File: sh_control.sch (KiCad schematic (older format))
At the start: 62 parts, among them IC5 LM317MDCY, J1 12401598E4#2A, J2 10129381-906001BLF, J3 10129381-906001BLF

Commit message: deleted all, beginning of eval board
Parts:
- removed C13: 1 uF, SamacSys_Parts:CAPC3216X210N, symbol SamacSys_Parts:SH31B105K500CT
- removed C14, C18, C19, C20, C21, C22, C23: 10 uF, SamacSys_Parts:CAPC3216X180N, symbol SamacSys_Parts:CL31A106KPHNNNE
- removed C15, C17: 0.1 uF, SamacSys_Parts:CAPC3216X88N, symbol SamacSys_Parts:C1206C104K5RAC7411
- removed C16, C24, C25, C26, C27: 100 uF, SamacSys_Parts:CAPPRD250W45D630H500, symbol SamacSys_Parts:10ML100MEFC6.3X5
- removed D1, D2, D3: FM4002-W, SamacSys_Parts:DIOM5025X231N, symbol SamacSys_Parts:FM4002-W
- removed DN_1, DN_2, DN_3, DN_4, DP_1, DP_2, DP_3, DP_4, GND1, GND2, GND_1, GND_2, GND_3, GND_4, LED_VCC_in1, LED_VCC_out1, VCC_1, VCC_2, VCC_3, VCC_4: TestPoint, TestPoint:TestPoint_Pad_2.0x2.0mm, symbol Connector:TestPoint
- removed F1, F2: Fuse, SamacSys_Parts:FUSC4632X85N, symbol SamacSys_Parts:MF-MSMF050-2
- removed H1, H2, H3, H4: MountingHole, MountingHole:MountingHole_3.2mm_M3, symbol Mechanical:MountingHole
- removed IC5: LM317MDCY, SamacSys_Parts:SOT230P700X180-4N, symbol SamacSys_Parts:LM317MDCY
- removed J1: 12401598E4#2A, usb c connector:AMPHENOL_12401598E4#2A, symbol 12401598E4_2A:12401598E4#2A
- removed J2, J3: 10129381-906001BLF, SamacSys_Parts:HDRV6W67P254_2X3_762X483X858P, symbol SamacSys_Parts:10129381-906001BLF
- removed LED4, LED5, LED6, LED7, LED8, LED9: COM-13667, SamacSys_Parts:COM13667, symbol SamacSys_Parts:COM-13667
- removed R31, R33: 390 R, SamacSys_Parts:RESC3216X60N, symbol SamacSys_Parts:CRCW1206390RFKEA
- removed R32: 240 R, SamacSys_Parts:RESC3216X75N, symbol SamacSys_Parts:CR1206-FX-2400ELF
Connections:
- net labels removed: +3.3V, +5V, DN_1, DN_2, DN_3, DN_4, DN_hub, DP_1, DP_2, DP_3, DP_4, DP_hub, USB_GND, USB_vbus
- wire segments 213 -> 10
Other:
- moved on the sheet: PB0, PC5, PD2, PD3, PD7

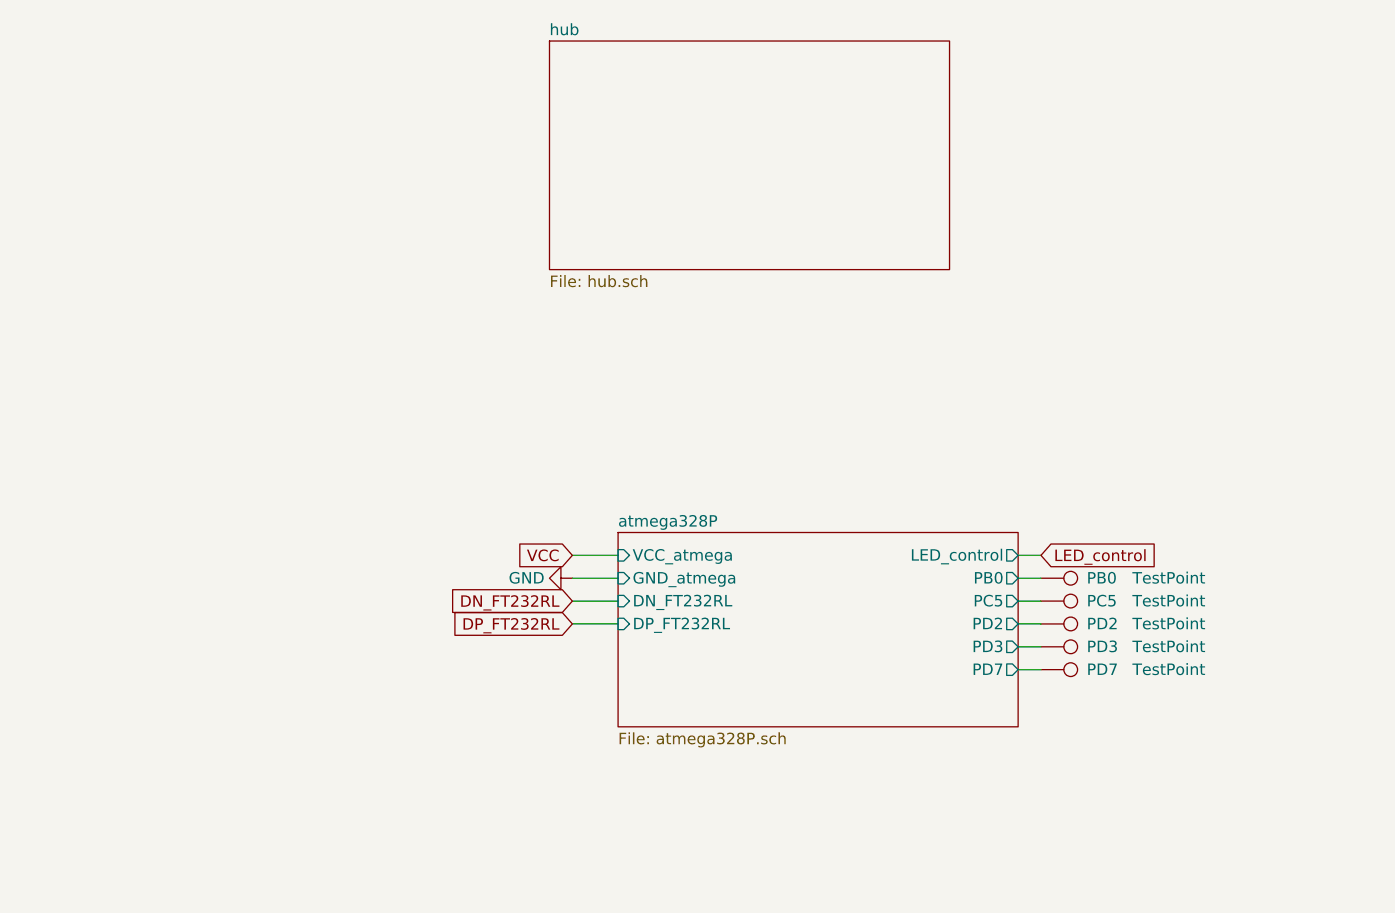
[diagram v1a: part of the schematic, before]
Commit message: hub schematic finished
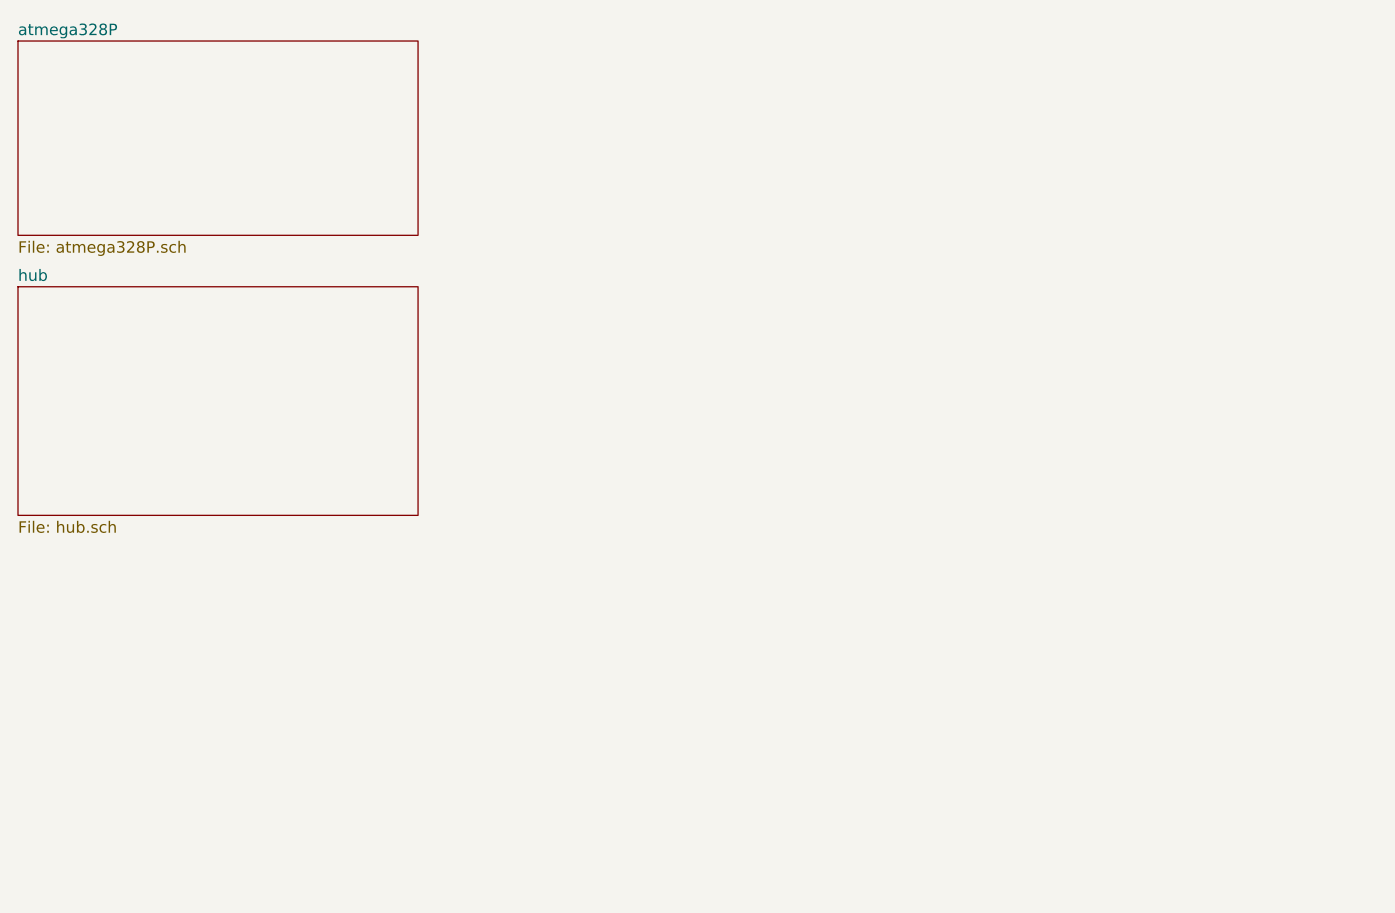
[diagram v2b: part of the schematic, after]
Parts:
- removed PB0, PC5, PD2, PD3, PD7: TestPoint, TestPoint:TestPoint_Pad_2.0x2.0mm, symbol Connector:TestPoint
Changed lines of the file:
@@
 $EndDescr
 $Sheet
-S 3250 2850 1750 850
+S 625  700  1750 850
 U 60A55B56
 F0 "atmega328P" 50
 F1 "atmega328P.sch" 50
-F2 "VCC_atmega" I L 3250 2950 50
-F3 "GND_atmega" I L 3250 3050 50
-F4 "LED_control" O R 5000 2950 50
-F5 "PB0" O R 5000 3050 50
-F6 "PC5" O R 5000 3150 50
-F7 "PD7" O R 5000 3450 50
-F8 "PD3" O R 5000 3350 50
-F9 "PD2" O R 5000 3250 50
-F10 "DN_FT232RL" I L 3250 3150 50
-F11 "DP_FT232RL" I L 3250 3250 50
 $EndSheet
-Text GLabel 5100 2950 2    50   Input ~ 0
-LED_control
-Wire Wire Line
-	5000 2950 5100 2950
 $Comp
 L power:GND #PWR0139
@@
 	1    0    0    -1
 $EndComp
-Text GLabel 3050 3150 0    50   Input ~ 0
-DN_FT232RL
-Text GLabel 3050 3250 0    50   Input ~ 0
-DP_FT232RL
-Wire Wire Line
-	3050 3150 3250 3150
-Wire Wire Line
-	3050 3250 3250 3250
-$Comp
-L power:GND #PWR0148
-U 1 1 6076ABFB
-P 3050 3050
-F 0 "#PWR0148" H 3050 2800 50  0001 C CNN
-F 1 "GND" V 3050 2850 50  0000 C CNN
-F 2 "" H 3050 3050 50  0001 C CNN
-F 3 "" H 3050 3050 50  0001 C CNN
-	1    3050 3050
-	0    1    1    0
-$EndComp
-Wire Wire Line
-	3050 3050 3250 3050
-Text GLabel 3050 2950 0    50   Input ~ 0
-VCC
-Wire Wire Line
-	3050 2950 3250 2950
-$Comp
-L Connector:TestPoint PB0
-U 1 1 60793E9F
-P 5100 3050
-F 0 "PB0" V 5100 3250 50  0000 L CNN
-F 1 "TestPoint" V 5100 3450 50  0000 L CNN
-F 2 "TestPoint:TestPoint_Pad_2.0x2.0mm" H 5300 3050 50  0001 C CNN
-F 3 "~" H 5300 3050 50  0001 C CNN
-	1    5100 3050
-	0    1    1    0
-$EndComp
-$Comp
-L Connector:TestPoint PC5
-U 1 1 607EDBC8
-P 5100 3150
-F 0 "PC5" V 5100 3350 50  0000 L CNN
-F 1 "TestPoint" V 5100 3550 50  0000 L CNN
-F 2 "TestPoint:TestPoint_Pad_2.0x2.0mm" H 5300 3150 50  0001 C CNN
-F 3 "~" H 5300 3150 50  0001 C CNN
-	1    5100 3150
-	0    1    1    0
-$EndComp
-$Comp
-L Connector:TestPoint PD2
-U 1 1 607F7B9C
-P 5100 3250
-F 0 "PD2" V 5100 3450 50  0000 L CNN
-F 1 "TestPoint" V 5100 3650 50  0000 L CNN
-F 2 "TestPoint:TestPoint_Pad_2.0x2.0mm" H 5300 3250 50  0001 C CNN
-F 3 "~" H 5300 3250 50  0001 C CNN
-	1    5100 3250
-	0    1    1    0
-$EndComp
-$Comp
-L Connector:TestPoint PD3
-U 1 1 608018E8
-P 5100 3350
-F 0 "PD3" V 5100 3550 50  0000 L CNN
-F 1 "TestPoint" V 5100 3750 50  0000 L CNN
-F 2 "TestPoint:TestPoint_Pad_2.0x2.0mm" H 5300 3350 50  0001 C CNN
-F 3 "~" H 5300 3350 50  0001 C CNN
-	1    5100 3350
-	0    1    1    0
-$EndComp
-$Comp
-L Connector:TestPoint PD7
-U 1 1 6080B6FE
-P 5100 3450
-F 0 "PD7" V 5100 3650 50  0000 L CNN
-F 1 "TestPoint" V 5100 3850 50  0000 L CNN
-F 2 "TestPoint:TestPoint_Pad_2.0x2.0mm" H 5300 3450 50  0001 C CNN
-F 3 "~" H 5300 3450 50  0001 C CNN
-	1    5100 3450
-	0    1    1    0
-$EndComp
-Wire Wire Line
-	5000 3050 5100 3050
-Wire Wire Line
-	5000 3150 5100 3150
-Wire Wire Line
-	5100 3250 5000 3250
-Wire Wire Line
-	5000 3350 5100 3350
-Wire Wire Line
-	5100 3450 5000 3450
 $Sheet
-S 2950 700  1750 1000
+S 625  1775 1750 1000
 U 606F0FFF
 F0 "hub" 50

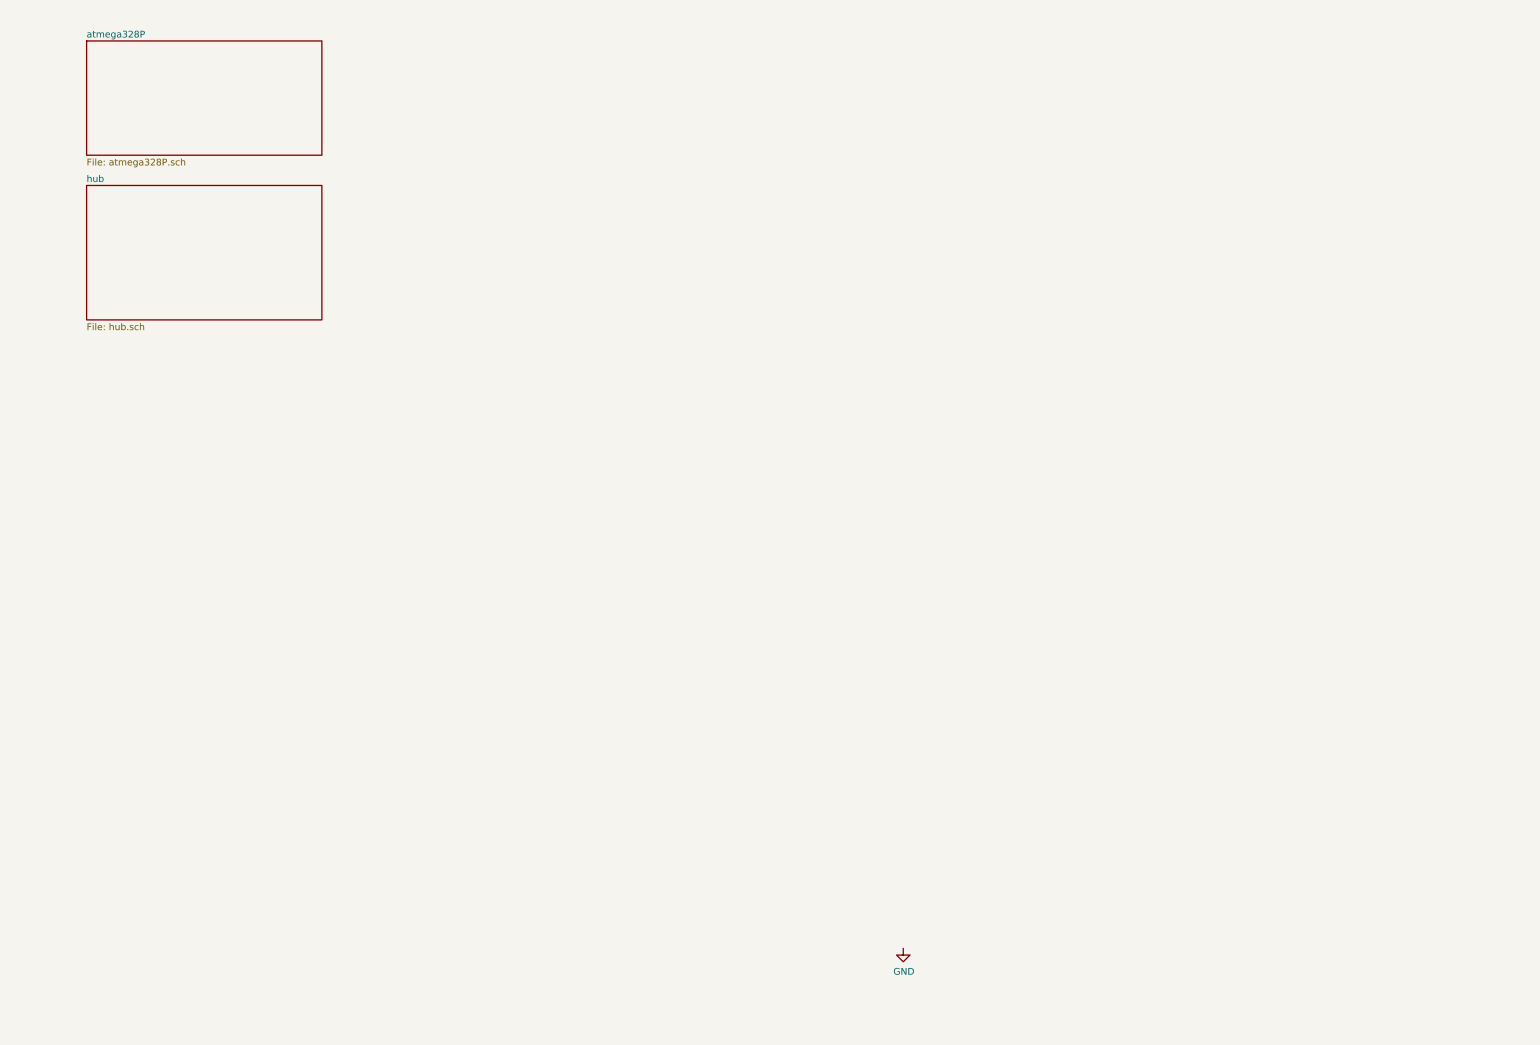
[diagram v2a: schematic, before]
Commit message: split in two boards from now on
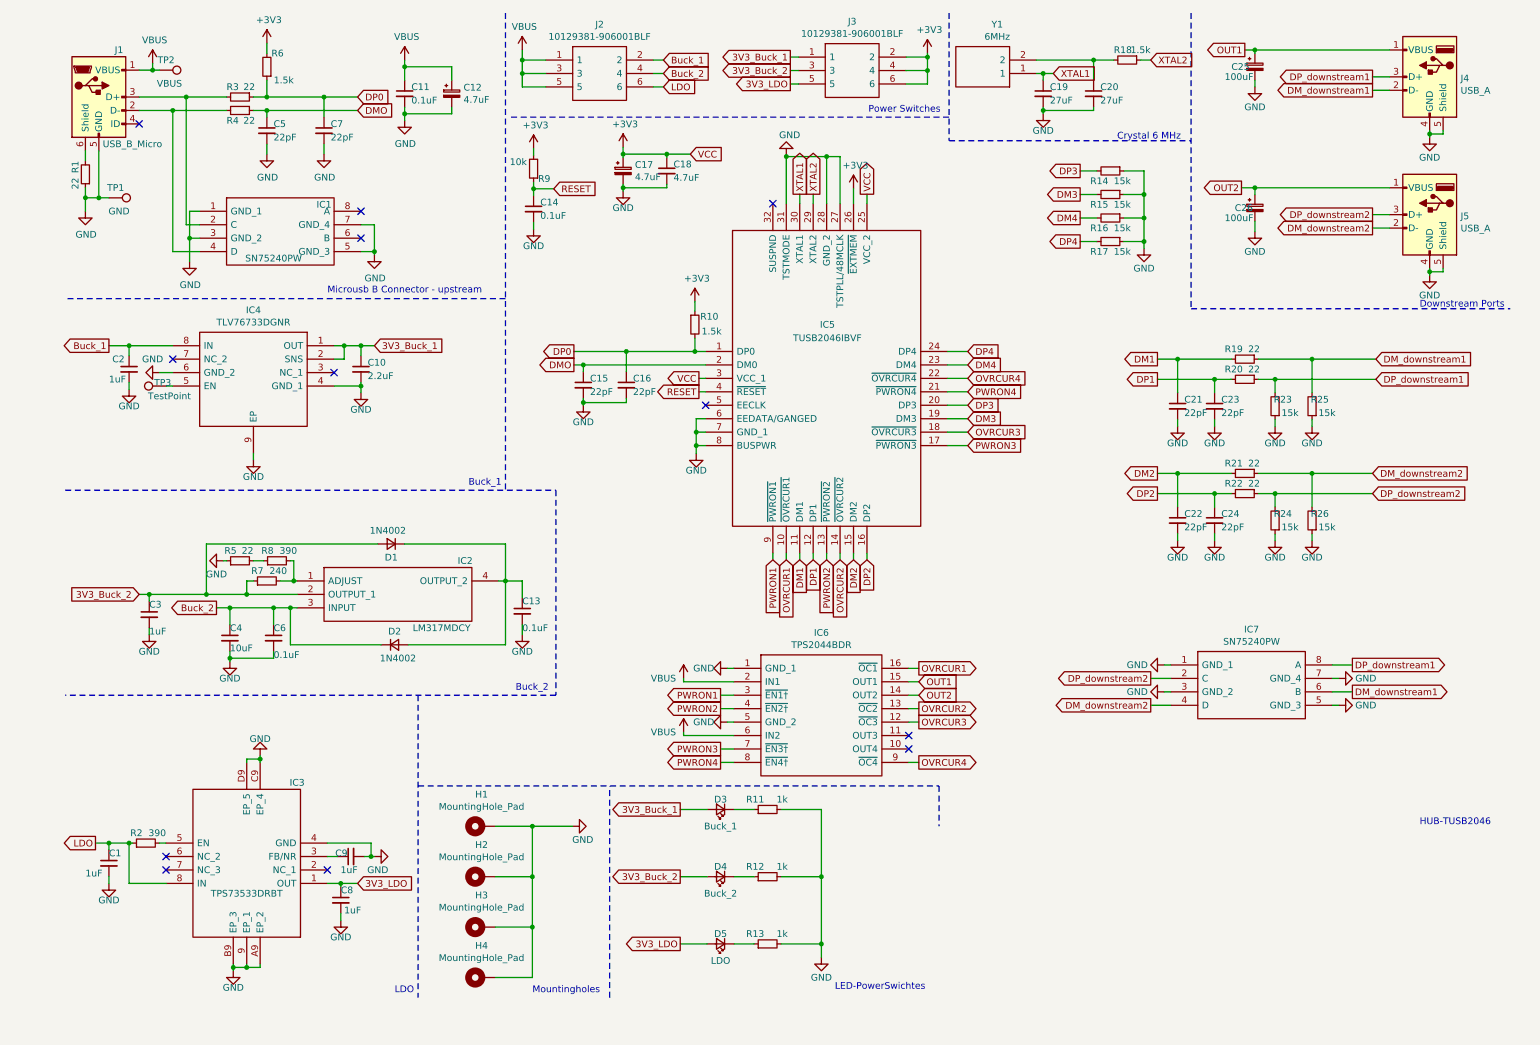
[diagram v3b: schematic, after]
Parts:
- added C1, C2, C3, C8, C9: 1uF, storage:C_1uF, symbol Device:C_Small
- added C10: 2.2uF, storage:C_2.2F, symbol Device:C_Small
- added C11, C13, C14, C6: 0.1uF, storage:C_0.1uF, symbol Device:C_Small
- added C12, C17: 4.7uF, storage:C_4.7uF, symbol Device:CP_Small
- added C15, C16, C21, C22, C23, C24, C5, C7: 22pF, storage:C_22pF, symbol Device:C_Small
- added C18: 4.7uF, storage:C_4.7uF, symbol Device:C_Small
- added C19, C20: 27uF, storage:C_27pF, symbol Device:C_Small
- added C25, C26: 100uF, storage:C_100uF, symbol Device:CP_Small
- added C4: 10uF, storage:C_10uF, symbol Device:C_Small
- added D1, D2: 1N4002, storage:D_1N4002, symbol Device:D_Small
- added D3: Buck_1, SamacSys_Parts:LEDC3214X78N, symbol Device:LED_Small
- added D4: Buck_2, SamacSys_Parts:LEDC3214X78N, symbol Device:LED_Small
- added D5: LDO, SamacSys_Parts:LEDC3214X78N, symbol Device:LED_Small
- added H1, H2, H3, H4: MountingHole_Pad, MountingHole:MountingHole_3.2mm_M3_Pad_Via, symbol Mechanical:MountingHole_Pad
- added IC1, IC7: SN75240PW, SamacSys_Parts:SOP65P640X120-8N, symbol SamacSys_Parts:SN75240PW
- added IC2: LM317MDCY, SamacSys_Parts:SOT230P700X180-4N, symbol SamacSys_Parts:LM317MDCY
- added IC3: TPS73533DRBT, SamacSys_Parts:TPS73533DRBT, symbol SamacSys_Parts:TPS73533DRBT
- added IC4: TLV76733DGNR, SamacSys_Parts:SOP65P490X110-9N, symbol SamacSys_Parts:TLV76733DGNR
- added IC5: TUSB2046IBVF, SamacSys_Parts:QFP80P900X900X160-32N, symbol SamacSys_Parts:TUSB2046IBVF
- added IC6: TPS2044BDR, SamacSys_Parts:SOIC127P600X175-16N, symbol SamacSys_Parts:TPS2044BDR
- added J1: USB_B_Micro, Connector_USB:USB_Micro-B_Molex-105017-0001, symbol Connector:USB_B_Micro
- added J2, J3: 10129381-906001BLF, SamacSys_Parts:HDRV6W67P254_2X3_762X483X858P, symbol SamacSys_Parts:10129381-906001BLF
- added J4, J5: USB_A, Connector_USB:USB_A_Molex_67643_Horizontal, symbol Connector:USB_A
- added R1, R19, R20, R21, R22, R3, R4, R5: 22, storage:R_22, symbol Device:R_Small
- added R10, R18, R6: 1.5k, storage:R_1K5, symbol Device:R_Small
- added R11, R12, R13: 1k, storage:R_1K, symbol Device:R_Small
- added R14, R15, R16, R17, R23, R24, R25, R26: 15k, storage:R_15K, symbol Device:R_Small
- added R2, R8: 390, storage:R_390, symbol Device:R_Small
- added R7: 240, storage:R_240, symbol Device:R_Small
- added R9: 10k, storage:R_10K, symbol Device:R_Small
- added TP1: GND, TestPoint:TestPoint_Pad_D2.5mm, symbol Connector:TestPoint
- added TP2: VBUS, TestPoint:TestPoint_Pad_D2.5mm, symbol Connector:TestPoint
- added TP3: TestPoint, TestPoint:TestPoint_Pad_D2.5mm, symbol Connector:TestPoint
- added Y1: 6MHz, SamacSys_Parts:LFXTAL036567BULK, symbol SamacSys_Parts:LFXTAL036567BULK
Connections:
- net GND: now also C1.2, C10.2, C11.2, C12.2, C13.2, C14.2, C15.2, C16.2, C17.2, C18.2, C19.2, C2.2, C20.2, C21.2, C22.2, C23.2, C24.2, C25.2, C26.2, C3.2, C4.2, C5.2, C6.2, C7.2, C8.2, C9.2, H1.1, H2.1, H3.1, H4.1, IC1.1 (GND_1), IC1.3 (GND_2), IC1.5 (GND_3), IC1.7 (GND_4), IC3.4 (GND), IC3.9 (EP_1), IC3.A9 (EP_2), IC3.B9 (EP_3), IC3.C9 (EP_4), IC3.D9 (EP_5), IC4.4 (GND_1), IC4.6 (GND_2), IC4.9 (EP), IC5.27 (TSTPLL/48MCLK), IC5.28 (GND_2), IC5.31 (TSTMODE), IC5.6 (EEDATA/GANGED), IC5.7 (GND_1), IC5.8 (BUSPWR), IC6.1 (GND_1), IC6.5 (GND_2), IC7.1 (GND_1), IC7.3 (GND_2), IC7.5 (GND_3), IC7.7 (GND_4), J1.5 (GND), J4.4 (GND), J4.5 (Shield), J5.4 (GND), J5.5 (Shield), R1.1, R11.2, R12.2, R13.2, R14.1, R15.1, R16.1, R17.1, R23.1, R24.1, R25.1, R26.1, R5.1, TP1.1
- new net: IC4.5 (EN), TP3.1
- new net: IC2.1 (ADJUST), R7.2, R8.2
- new net: C13.1, D1.1 (K), D2.2 (A), IC2.4 (OUTPUT_2)
- new net: R5.2, R8.1
- new net: C9.1, IC3.3 (FB/NR)
- new net: IC3.5 (EN), R2.2
- new net: C20.1, R18.2, Y1.2
- new net: J1.6 (Shield), R1.2
- new net: IC1.2 (C), J1.3 (D+), R3.2
- new net: IC1.4 (D), J1.2 (D-), R4.2
- new net: D3.1 (K), R11.1
- new net: D4.1 (K), R12.1
- new net: D5.1 (K), R13.1
- new net +3V3: C17.1, C18.1, IC5.25 (VCC_2), IC5.26 (~EXTMEM), IC5.3 (VCC_1), J3.2, J3.4, J3.6, R10.1, R6.2, R9.2
- new net 3V3_Buck_1: C10.1, D3.2 (A), IC4.1 (OUT), IC4.2 (SNS), J3.1
- new net 3V3_Buck_2: C3.1, D1.2 (A), D4.2 (A), IC2.2 (OUTPUT_1), J3.3, R7.1
- new net 3V3_LDO: C8.1, D5.2 (A), IC3.1 (OUT), J3.5
- new net Buck_1: C2.1, IC4.8 (IN), J2.2
- new net Buck_2: C4.1, C6.1, D2.1 (K), IC2.3 (INPUT), J2.4
- new net DM1: C21.1, IC5.11 (DM1), R19.2
- new net DM2: C22.1, IC5.15 (DM2), R21.2
- new net DM3: IC5.19 (DM3), R15.2
- new net DM4: IC5.23 (DM4), R16.2
- new net DMO: C15.1, C5.1, IC5.2 (DM0), R4.1
- new net DM_downstream1: IC7.6 (B), J4.2 (D-), R19.1, R25.2
- new net DM_downstream2: IC7.4 (D), J5.2 (D-), R21.1, R26.2
- new net DP0: C16.1, C7.1, IC5.1 (DP0), R10.2, R3.1, R6.1
- new net DP1: C23.1, IC5.12 (DP1), R20.2
- new net DP2: C24.1, IC5.16 (DP2), R22.2
- new net DP3: IC5.20 (DP3), R14.2
- new net DP4: IC5.24 (DP4), R17.2
- new net DP_downstream1: IC7.8 (A), J4.3 (D+), R20.1, R23.2
- new net DP_downstream2: IC7.2 (C), J5.3 (D+), R22.1, R24.2
- new net LDO: C1.1, IC3.8 (IN), J2.6, R2.1
- new net OUT1: C25.1, IC6.15 (OUT1), J4.1 (VBUS)
- new net OUT2: C26.1, IC6.14 (OUT2), J5.1 (VBUS)
- new net OVRCUR1: IC5.10 (~OVRCUR1), IC6.16 (~OC1)
- new net OVRCUR2: IC5.14 (~OVRCUR2), IC6.13 (~OC2)
- new net OVRCUR3: IC5.18 (~OVRCUR3), IC6.12 (~OC3)
- new net OVRCUR4: IC5.22 (~OVRCUR4), IC6.9 (~OC4)
- new net PWRON1: IC5.9 (~PWRON1), IC6.3 (~EN1†)
- new net PWRON2: IC5.13 (~PWRON2), IC6.4 (~EN2†)
- new net PWRON3: IC5.17 (~PWRON3), IC6.7 (~EN3†)
- new net PWRON4: IC5.21 (~PWRON4), IC6.8 (~EN4†)
- new net RESET: C14.1, IC5.4 (~RESET), R9.1
- new net VBUS: C11.1, C12.1, IC6.2 (IN1), IC6.6 (IN2), J1.1 (VBUS), J2.1, J2.3, J2.5, TP2.1
- new net XTAL1: C19.1, IC5.30 (XTAL1), Y1.1
- new net XTAL2: IC5.29 (XTAL2), R18.1
- no-connect marks 0 -> 12
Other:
- note added: "Buck_1\n"
- note added: "Buck_2\n"
- note added: "Crystal 6 MHz"
- note added: "Downstream Ports"
- note added: "HUB-TUSB2046"
- note added: "LDO"
- note added: "LED-PowerSwichtes"
- note added: "Microusb B Connector - upstream\n\n"
- note added: "Mountingholes"
- note added: "Power Switches"
